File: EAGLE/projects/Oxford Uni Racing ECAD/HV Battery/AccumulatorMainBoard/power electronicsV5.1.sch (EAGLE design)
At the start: 82 parts, among them IC1 4043D, IC2 SE555D, IC9 4011D, K2 T9AS5D12-12=T9A, K6 T9AS1D12-48=T9A, K7 T9AS1D12-48=T9A, Q1 BSS138, Q2 BSS138, Q3 BSS138, Q4 BSS138

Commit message: Final final mainboard Design (v5.1)
Adds termination resistors to Can 1. Updates silkscreen. Connects Power plane islands. 
Passes design rule check, verified the CAM files using PCBway gerber viewer

To do list (if have time): 
change to resettable fuses; add OUR logo (haven't figured out how)
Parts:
- added R13, R16: 120, rcl:R-EU_R1206
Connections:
- net CAN1_H: now also R13.1, R16.1
- net CAN1_L: now also R13.2, R16.2

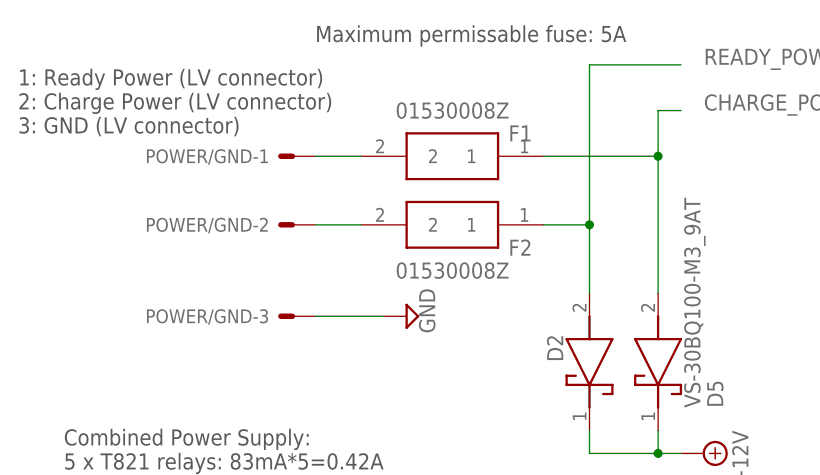
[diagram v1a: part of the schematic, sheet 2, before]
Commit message: FINAL FINLAL FINAL mainboard design
Changes the fuses from car fuses to 2.5A resettable fuses. Adds the OUR logo and designers. Moves LED to more logical locations
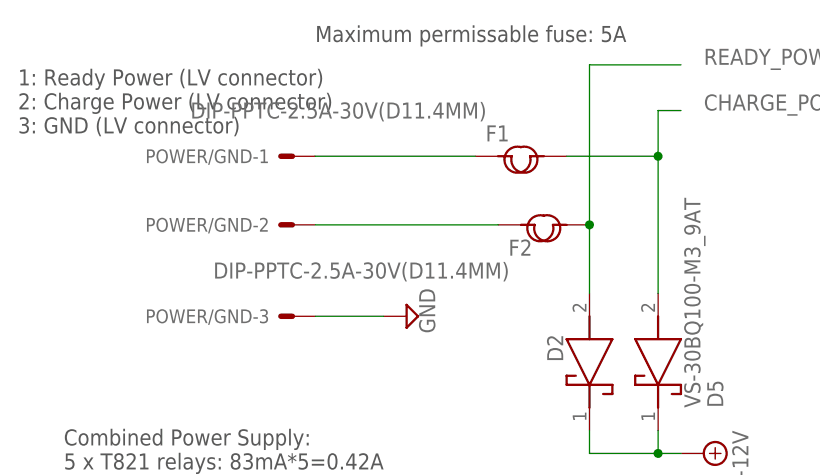
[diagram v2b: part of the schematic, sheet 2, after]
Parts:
- C1: POPULARITY (none) -> 88F
- F1, F2: value 01530008Z -> DIP-PPTC-2.5A-30V(D11.4MM); device SamacSys_Parts:01530008Z -> DIP-PPTC-2.5A-30V_D11.4MM_:DIP-PPTC-2.5A-30V(D11.4MM)
- renumbered LED4 to LED4-DISCHARGE-ENABLE, LED5 to LED5-CHARGE-SAFE
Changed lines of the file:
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@@
 <part name="+3V4" library="supply1" library_urn="urn:adsk.eagle:library:371" deviceset="+3V3" device=""/>
 <part name="SUPPLY2" library="supply2" library_urn="urn:adsk.eagle:library:372" deviceset="GND" device=""/>
-<part name="C1" library="rcl" library_urn="urn:adsk.eagle:library:334" deviceset="C-EU" device="C0805" package3d_urn="urn:adsk.eagle:package:23617/2" value="0.1uF"/>
+<part name="C1" library="rcl" library_urn="urn:adsk.eagle:library:334" deviceset="C-EU" device="C0805" package3d_urn="urn:adsk.eagle:package:23617/2" value="0.1uF">
+<spice>
+<pinmapping spiceprefix="C">
+<pinmap gate="G$1" pin="1" pinorder="1"/>
+<pinmap gate="G$1" pin="2" pinorder="2"/>
+</pinmapping>
+</spice>
+<attribute name="POPULARITY" value="88F"/>
+</part>
 <part name="C2" library="rcl" library_urn="urn:adsk.eagle:library:334" deviceset="C-EU" device="C0805" package3d_urn="urn:adsk.eagle:package:23617/2" value="0.1uF"/>
 <part name="C3" library="rcl" library_urn="urn:adsk.eagle:library:334" deviceset="C-EU" device="C0805" package3d_urn="urn:adsk.eagle:package:23617/2" value="0.1uF"/>
 <part name="SUPPLY11" library="supply2" library_urn="urn:adsk.eagle:library:372" deviceset="GND" device=""/>
 <part name="+3V3" library="supply1" library_urn="urn:adsk.eagle:library:371" deviceset="+3V3" device=""/>
-<part name="LED4" library="led" library_urn="urn:adsk.eagle:library:259" deviceset="LED" device="SML0805" package3d_urn="urn:adsk.eagle:package:15830/1"/>
-<part name="LED5" library="led" library_urn="urn:adsk.eagle:library:259" deviceset="LED" device="SML0805" package3d_urn="urn:adsk.eagle:package:15830/1"/>
+<part name="LED4-DISCHARGE-ENABLE" library="led" library_urn="urn:adsk.eagle:library:259" deviceset="LED" device="SML0805" package3d_urn="urn:adsk.eagle:package:15830/1"/>
+<part name="LED5-CHARGE-SAFE" library="led" library_urn="urn:adsk.eagle:library:259" deviceset="LED" device="SML0805" package3d_urn="urn:adsk.eagle:package:15830/1"/>
 <part name="LED6" library="led" library_urn="urn:adsk.eagle:library:259" deviceset="LED" device="SML0805" package3d_urn="urn:adsk.eagle:package:15830/1"/>
 <part name="SUPPLY4" library="supply2" library_urn="urn:adsk.eagle:library:372" deviceset="+12V" device=""/>
 <part name="SUPPLY22" library="supply2" library_urn="urn:adsk.eagle:library:372" deviceset="GND" device=""/>
-<part name="F1" library="SamacSys_Parts" deviceset="01530008Z" device=""/>
-<part name="F2" library="SamacSys_Parts" deviceset="01530008Z" device=""/>
+<part name="F1" library="DIP-PPTC-2.5A-30V_D11.4MM_" deviceset="DIP-PPTC-2.5A-30V(D11.4MM)" device=""/>
+<part name="F2" library="DIP-PPTC-2.5A-30V_D11.4MM_" deviceset="DIP-PPTC-2.5A-30V(D11.4MM)" device=""/>
 <part name="SUPPLY15" library="supply2" library_urn="urn:adsk.eagle:library:372" deviceset="+12V" device=""/>
 <part name="SUPPLY25" library="supply2" library_urn="urn:adsk.eagle:library:372" deviceset="GND" device=""/>
@@
 <instance part="R6" gate="G$1" x="-15.24" y="68.58" smashed="yes" rot="R270">
 <attribute name="NAME" x="-13.7414" y="72.39" size="1.778" layer="95" rot="R270"/>
-<attribute name="VALUE" x="-18.542" y="64.77" size="1.778" layer="96" rot="R270"/>
+<attribute name="VALUE" x="-10.922" y="72.39" size="1.778" layer="96" rot="R270"/>
 </instance>
 <instance part="R7" gate="G$1" x="-20.32" y="68.58" smashed="yes" rot="R270">
@@
 <attribute name="VALUE" x="-53.34" y="-25.4" size="1.778" layer="96" rot="MR0"/>
 </instance>
-<instance part="LED4" gate="G$1" x="-20.32" y="58.42" smashed="yes">
+<instance part="LED4-DISCHARGE-ENABLE" gate="G$1" x="-20.32" y="58.42" smashed="yes">
 <attribute name="NAME" x="-16.764" y="53.848" size="1.778" layer="95" rot="R90"/>
 <attribute name="VALUE" x="-14.605" y="53.848" size="1.778" layer="96" rot="R90"/>
 </instance>
-<instance part="LED5" gate="G$1" x="-15.24" y="58.42" smashed="yes">
+<instance part="LED5-CHARGE-SAFE" gate="G$1" x="-15.24" y="58.42" smashed="yes">
 <attribute name="NAME" x="-11.684" y="53.848" size="1.778" layer="95" rot="R90"/>
 <attribute name="VALUE" x="-9.525" y="53.848" size="1.778" layer="96" rot="R90"/>
@@
 </instance>
 <instance part="R14" gate="G$1" x="162.56" y="101.6" smashed="yes" rot="MR90">
-<attribute name="NAME" x="164.0586" y="97.79" size="1.778" layer="95" rot="MR90"/>
+<attribute name="NAME" x="164.0586" y="99.822" size="1.778" layer="95" rot="MR90"/>
 <attribute name="VALUE" x="159.258" y="97.79" size="1.778" layer="96" rot="MR90"/>
+<attribute name="POPULARITY" x="159.512" y="100.33" size="1.778" layer="96" rot="MR90"/>
 </instance>
 <instance part="LED7" gate="G$1" x="162.56" y="91.44" smashed="yes">
@@
 </segment>
 <segment>
-<pinref part="LED4" gate="G$1" pin="C"/>
+<pinref part="LED4-DISCHARGE-ENABLE" gate="G$1" pin="C"/>
 <wire x1="-20.32" y1="53.34" x2="-20.32" y2="35.56" width="0.1524" layer="91"/>
 <pinref part="IC9" gate="D" pin="I1"/>
@@
 <pinref part="IC9" gate="D" pin="I0"/>
 <wire x1="-17.78" y1="40.64" x2="-15.24" y2="40.64" width="0.1524" layer="91"/>
-<pinref part="LED5" gate="G$1" pin="C"/>
+<pinref part="LED5-CHARGE-SAFE" gate="G$1" pin="C"/>
 <wire x1="-15.24" y1="40.64" x2="-12.7" y2="40.64" width="0.1524" layer="91"/>
 <wire x1="-15.24" y1="53.34" x2="-15.24" y2="40.64" width="0.1524" layer="91"/>
@@
 <segment>
 <pinref part="R7" gate="G$1" pin="2"/>
-<pinref part="LED4" gate="G$1" pin="A"/>
+<pinref part="LED4-DISCHARGE-ENABLE" gate="G$1" pin="A"/>
 <wire x1="-20.32" y1="60.96" x2="-20.32" y2="63.5" width="0.1524" layer="91"/>
 </segment>
@@
 <net name="N$26" class="0">
 <segment>
-<pinref part="LED5" gate="G$1" pin="A"/>
+<pinref part="LED5-CHARGE-SAFE" gate="G$1" pin="A"/>
 <pinref part="R6" gate="G$1" pin="2"/>
 <wire x1="-15.24" y1="60.96" x2="-15.24" y2="63.5" width="0.1524" layer="91"/>
@@
 <attribute name="VALUE" x="53.975" y="213.995" size="1.778" layer="96" rot="R90"/>
 </instance>
-<instance part="F1" gate="G$1" x="66.04" y="233.68" smashed="yes" rot="R180">
-<attribute name="NAME" x="64.77" y="236.22" size="1.778" layer="95" rot="R180" align="center-left"/>
-<attribute name="VALUE" x="62.23" y="238.76" size="1.778" layer="96" rot="R180" align="center-left"/>
+<instance part="F1" gate="G$1" x="63.5" y="233.68" smashed="yes" rot="R180">
+<attribute name="NAME" x="62.23" y="236.22" size="1.778" layer="95" rot="R180" align="center-left"/>
+<attribute name="VALUE" x="59.69" y="238.76" size="1.778" layer="96" rot="R180" align="center-left"/>
 </instance>
 <instance part="F2" gate="G$1" x="66.04" y="226.06" smashed="yes" rot="R180">
@@
 <segment>
 <wire x1="71.12" y1="226.06" x2="71.12" y2="218.44" width="0.1524" layer="91"/>
-<wire x1="66.04" y1="226.06" x2="71.12" y2="226.06" width="0.1524" layer="91"/>
 <junction x="71.12" y="226.06"/>
 <pinref part="F2" gate="G$1" pin="1"/>
@@
 <wire x1="78.74" y1="233.68" x2="78.74" y2="218.44" width="0.1524" layer="91"/>
 <pinref part="F1" gate="G$1" pin="1"/>
-<wire x1="66.04" y1="233.68" x2="78.74" y2="233.68" width="0.1524" layer="91"/>
+<wire x1="68.58" y1="233.68" x2="78.74" y2="233.68" width="0.1524" layer="91"/>
 <junction x="78.74" y="233.68"/>
 <label x="83.82" y="238.76" size="1.778" layer="95"/>
@@
 <pinref part="POWER/GND" gate="-2" pin="S"/>
 <pinref part="F2" gate="G$1" pin="2"/>
-<wire x1="40.64" y1="226.06" x2="45.72" y2="226.06" width="0.1524" layer="91"/>
+<wire x1="40.64" y1="226.06" x2="60.96" y2="226.06" width="0.1524" layer="91"/>
 </segment>
 </net>
@@
 <pinref part="POWER/GND" gate="-1" pin="S"/>
 <pinref part="F1" gate="G$1" pin="2"/>
-<wire x1="40.64" y1="233.68" x2="45.72" y2="233.68" width="0.1524" layer="91"/>
-</segment>
-</net>
+<wire x1="40.64" y1="233.68" x2="58.42" y2="233.68" width="0.1524" layer="91"/>
+</segment>
+</net>

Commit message: final fnl... mainbaord
yeah
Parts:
- renumbered LED4-DISCHARGE-ENABLE to LED4, LED5-CHARGE-SAFE to LED5
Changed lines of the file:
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@@
 <part name="SUPPLY11" library="supply2" library_urn="urn:adsk.eagle:library:372" deviceset="GND" device=""/>
 <part name="+3V3" library="supply1" library_urn="urn:adsk.eagle:library:371" deviceset="+3V3" device=""/>
-<part name="LED4-DISCHARGE-ENABLE" library="led" library_urn="urn:adsk.eagle:library:259" deviceset="LED" device="SML0805" package3d_urn="urn:adsk.eagle:package:15830/1"/>
-<part name="LED5-CHARGE-SAFE" library="led" library_urn="urn:adsk.eagle:library:259" deviceset="LED" device="SML0805" package3d_urn="urn:adsk.eagle:package:15830/1"/>
+<part name="LED4" library="led" library_urn="urn:adsk.eagle:library:259" deviceset="LED" device="SML0805" package3d_urn="urn:adsk.eagle:package:15830/1"/>
+<part name="LED5" library="led" library_urn="urn:adsk.eagle:library:259" deviceset="LED" device="SML0805" package3d_urn="urn:adsk.eagle:package:15830/1"/>
 <part name="LED6" library="led" library_urn="urn:adsk.eagle:library:259" deviceset="LED" device="SML0805" package3d_urn="urn:adsk.eagle:package:15830/1"/>
 <part name="SUPPLY4" library="supply2" library_urn="urn:adsk.eagle:library:372" deviceset="+12V" device=""/>
@@
 <attribute name="VALUE" x="-53.34" y="-25.4" size="1.778" layer="96" rot="MR0"/>
 </instance>
-<instance part="LED4-DISCHARGE-ENABLE" gate="G$1" x="-20.32" y="58.42" smashed="yes">
+<instance part="LED4" gate="G$1" x="-20.32" y="58.42" smashed="yes">
 <attribute name="NAME" x="-16.764" y="53.848" size="1.778" layer="95" rot="R90"/>
 <attribute name="VALUE" x="-14.605" y="53.848" size="1.778" layer="96" rot="R90"/>
 </instance>
-<instance part="LED5-CHARGE-SAFE" gate="G$1" x="-15.24" y="58.42" smashed="yes">
+<instance part="LED5" gate="G$1" x="-15.24" y="58.42" smashed="yes">
 <attribute name="NAME" x="-11.684" y="53.848" size="1.778" layer="95" rot="R90"/>
 <attribute name="VALUE" x="-9.525" y="53.848" size="1.778" layer="96" rot="R90"/>
@@
 </segment>
 <segment>
-<pinref part="LED4-DISCHARGE-ENABLE" gate="G$1" pin="C"/>
+<pinref part="LED4" gate="G$1" pin="C"/>
 <wire x1="-20.32" y1="53.34" x2="-20.32" y2="35.56" width="0.1524" layer="91"/>
 <pinref part="IC9" gate="D" pin="I1"/>
@@
 <pinref part="IC9" gate="D" pin="I0"/>
 <wire x1="-17.78" y1="40.64" x2="-15.24" y2="40.64" width="0.1524" layer="91"/>
-<pinref part="LED5-CHARGE-SAFE" gate="G$1" pin="C"/>
+<pinref part="LED5" gate="G$1" pin="C"/>
 <wire x1="-15.24" y1="40.64" x2="-12.7" y2="40.64" width="0.1524" layer="91"/>
 <wire x1="-15.24" y1="53.34" x2="-15.24" y2="40.64" width="0.1524" layer="91"/>
@@
 <segment>
 <pinref part="R7" gate="G$1" pin="2"/>
-<pinref part="LED4-DISCHARGE-ENABLE" gate="G$1" pin="A"/>
+<pinref part="LED4" gate="G$1" pin="A"/>
 <wire x1="-20.32" y1="60.96" x2="-20.32" y2="63.5" width="0.1524" layer="91"/>
 </segment>
@@
 <net name="N$26" class="0">
 <segment>
-<pinref part="LED5-CHARGE-SAFE" gate="G$1" pin="A"/>
+<pinref part="LED5" gate="G$1" pin="A"/>
 <pinref part="R6" gate="G$1" pin="2"/>
 <wire x1="-15.24" y1="60.96" x2="-15.24" y2="63.5" width="0.1524" layer="91"/>
